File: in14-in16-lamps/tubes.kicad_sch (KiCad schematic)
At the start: 21 parts, among them J4 Conn_01x02_Pin

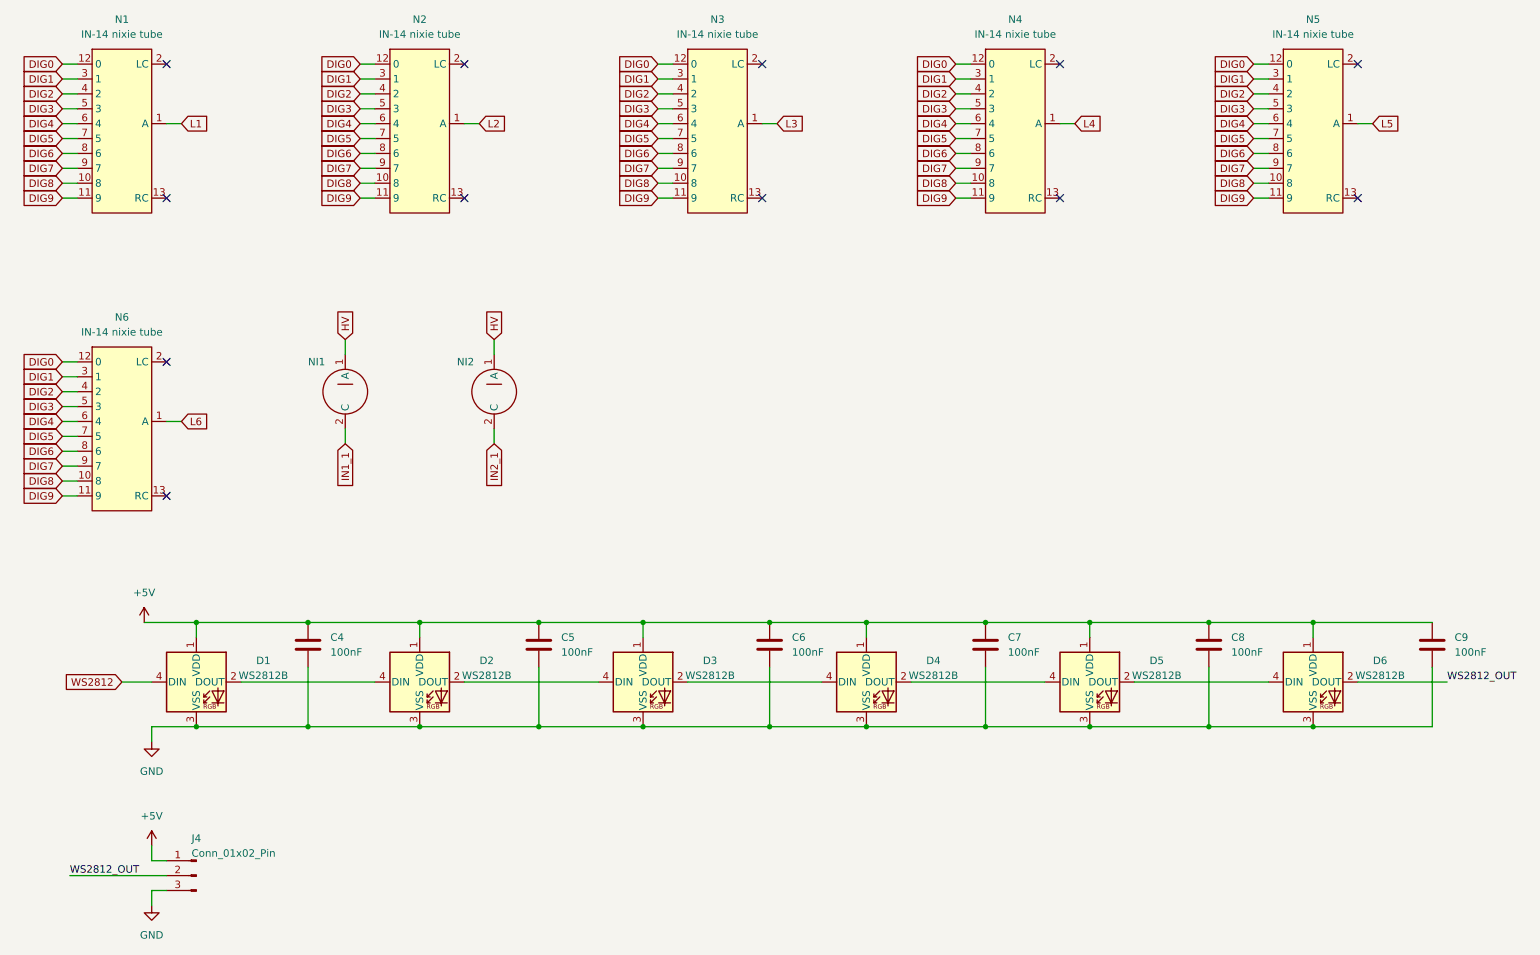
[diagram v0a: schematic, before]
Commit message: add in-14 and in-16 6 lamp version
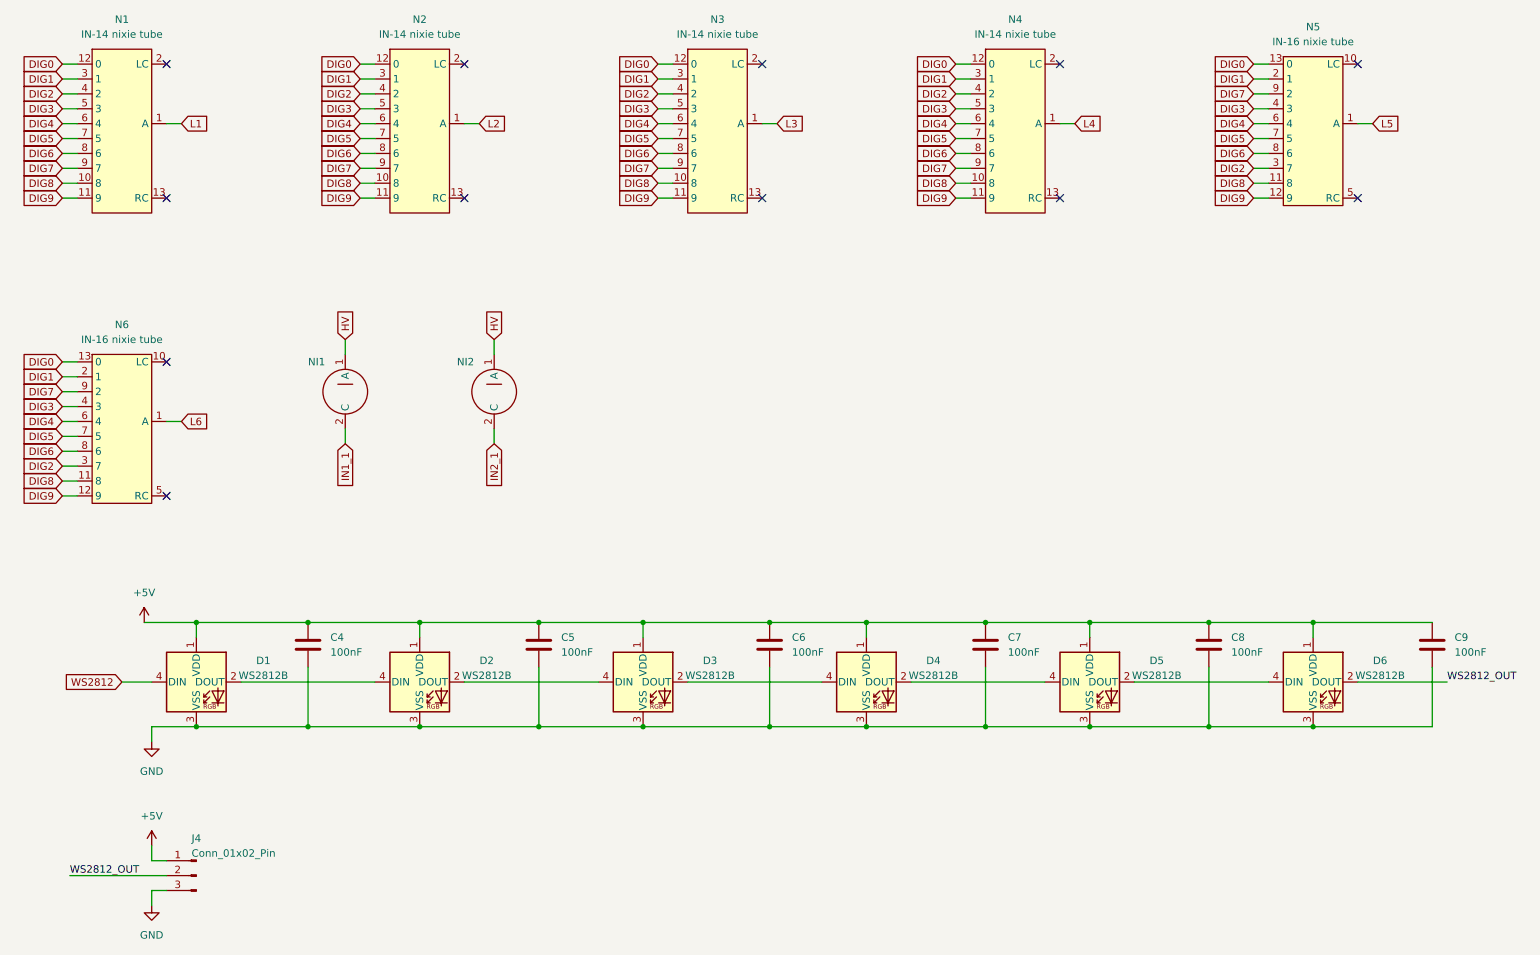
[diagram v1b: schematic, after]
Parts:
- removed N5, N6: IN-14 nixie tube, project_library:IN-14_nixie_tube, symbol project_library:IN-14_nixie_tube
- added N5, N6: IN-16 nixie tube, project_library:IN-16_nixie_tube, symbol project_library:IN-16_nixie_tube
- D1, D2, D3, D4, D5, D6: footprint LED_SMD:LED_WS2812B_PLCC4_5.0x5.0mm_P3.2mm -> project_library:SK6812_mini
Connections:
- net DIG0: now also N5.13 (0), N6.13 (0)
- net DIG1: now also N5.2 (1), N6.2 (1)
- net DIG2: now also N5.3 (7), N6.3 (7)
- net DIG3: now also N5.4 (3), N6.4 (3)
- net DIG4: now also N5.6 (4), N6.6 (4)
- net DIG5: now also N5.7 (5), N6.7 (5)
- net DIG6: now also N5.8 (6), N6.8 (6)
- net DIG7: now also N5.9 (2), N6.9 (2)
- net DIG8: now also N5.11 (8), N6.11 (8)
- net DIG9: now also N5.12 (9), N6.12 (9)
- net L5: now also N5.1 (A)
- net L6: now also N6.1 (A)
